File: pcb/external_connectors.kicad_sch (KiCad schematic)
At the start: 9 parts, among them J10 Conn_01x03_Pin, J11 Conn_01x03_Pin, J12 Conn_01x03_Pin, J13 Conn_01x03_Pin, J14 Conn_01x03_Pin, J15 Conn_02x10_Counter_Clockwise, J7 Conn_01x04_Pin_P2.54mm, J8 Conn_01x04_Qwiic, J9 Conn_01x03_Pin

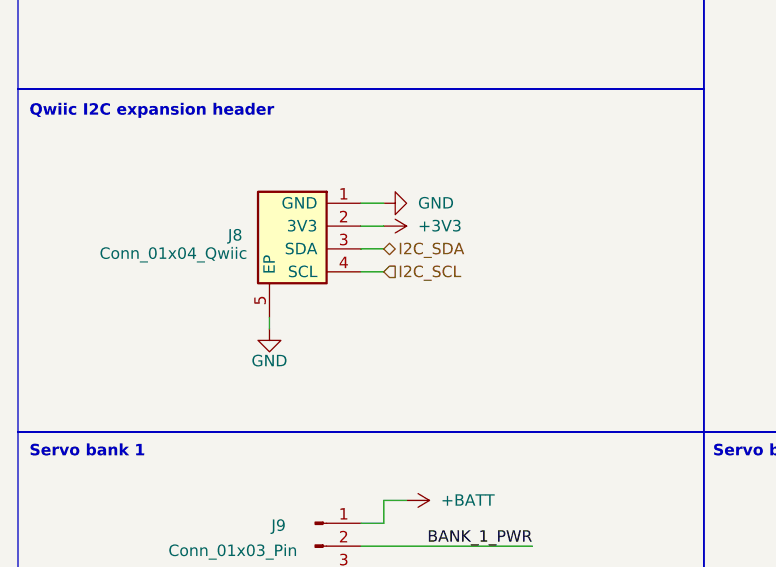
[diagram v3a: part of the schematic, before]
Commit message: Assign more footprints
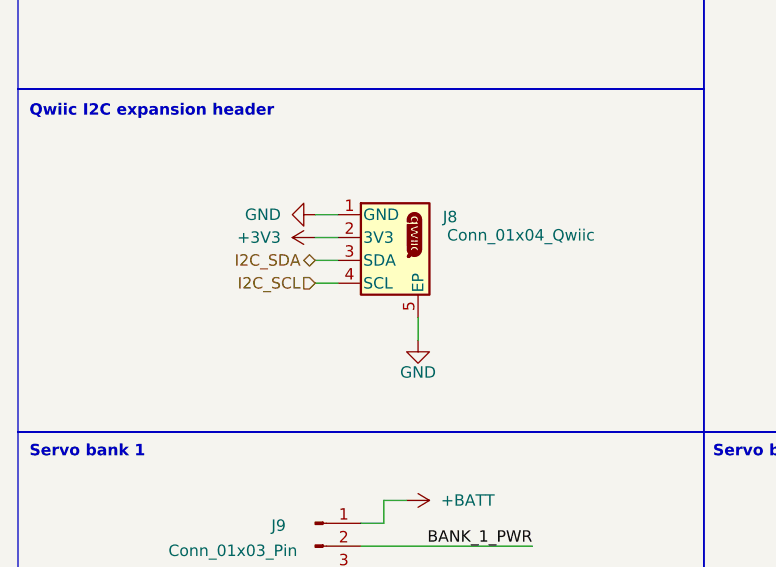
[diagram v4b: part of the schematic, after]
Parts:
- J8: footprint (none) -> Connector_JST:JST_SH_BM04B-SRSS-TB_1x04-1MP_P1.00mm_Vertical
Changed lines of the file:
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@@
 	(wire
 		(pts
-			(xy 50.8 71.12) (xy 53.34 71.12)
+			(xy 48.26 72.39) (xy 45.72 72.39)
 		)
 		(stroke
@@
 	(wire
 		(pts
-			(xy 40.64 77.47) (xy 40.64 76.2)
+			(xy 57.15 78.74) (xy 57.15 76.2)
 		)
 		(stroke
@@
 	(wire
 		(pts
-			(xy 50.8 66.04) (xy 53.34 66.04)
+			(xy 48.26 67.31) (xy 45.72 67.31)
 		)
 		(stroke
@@
 	(wire
 		(pts
-			(xy 50.8 68.58) (xy 53.34 68.58)
+			(xy 48.26 69.85) (xy 45.72 69.85)
 		)
 		(stroke
@@
 	(wire
 		(pts
-			(xy 50.8 63.5) (xy 53.34 63.5)
+			(xy 48.26 64.77) (xy 45.72 64.77)
 		)
 		(stroke
@@
 	(hierarchical_label "I2C_SCL"
 		(shape input)
-		(at 53.34 71.12 0)
+		(at 45.72 72.39 180)
 		(effects
 			(font
 				(size 1.27 1.27)
 			)
-			(justify left)
+			(justify right)
 		)
 	)
 	(hierarchical_label "I2C_SDA"
 		(shape bidirectional)
-		(at 53.34 68.58 0)
+		(at 45.72 69.85 180)
 		(effects
 			(font
 				(size 1.27 1.27)
 			)
-			(justify left)
+			(justify right)
 		)
 	)
@@
 	(symbol
 		(lib_id "Qwiic:Conn_01x04_Qwiic")
-		(at 45.72 66.04 0)
-		(mirror y)
+		(at 50.8 63.5 0)
 		(unit 1)
 		(exclude_from_sim no)
@@
 		(dnp no)
 		(property "Reference" "J8"
-			(at 36.83 67.056 0)
+			(at 60.706 65.024 0)
 			(effects
 				(font
@@
 		)
 		(property "Value" "Conn_01x04_Qwiic"
-			(at 29.972 69.088 0)
-			(effects
-				(font
-					(size 1.27 1.27)
-				)
-			)
-		)
-		(property "Footprint" ""
-			(at 45.72 66.04 0)
+			(at 68.58 67.056 0)
+			(effects
+				(font
+					(size 1.27 1.27)
+				)
+			)
+		)
+		(property "Footprint" "Connector_JST:JST_SH_BM04B-SRSS-TB_1x04-1MP_P1.00mm_Vertical"
+			(at 50.8 63.5 0)
 			(effects
 				(font
@@
 		)
 		(property "Datasheet" ""
-			(at 45.72 66.04 0)
-			(effects
-				(font
-					(size 1.27 1.27)
-				)
-				(hide yes)
-			)
-		)
-		(property "Description" "Qwiic I2C connector 4 pin"
-			(at 46.228 60.452 0)
+			(at 50.8 63.5 0)
+			(effects
+				(font
+					(size 1.27 1.27)
+				)
+				(hide yes)
+			)
+		)
+		(property "Description" "Qwiic I2C connector 4 pin, JST SH BM04B or JST SH SM04B"
+			(at 50.292 57.912 0)
 			(effects
 				(font
@@
 	(symbol
 		(lib_id "power:GND")
-		(at 53.34 63.5 90)
+		(at 45.72 64.77 270)
+		(mirror x)
 		(unit 1)
 		(exclude_from_sim no)
@@
 		(fields_autoplaced yes)
 		(property "Reference" "#PWR087"
-			(at 59.69 63.5 0)
+			(at 39.37 64.77 0)
 			(effects
 				(font
@@
 		)
 		(property "Value" "GND"
-			(at 57.15 63.4999 90)
+			(at 41.91 64.7699 90)
 			(effects
 				(font
@@
 		)
 		(property "Footprint" ""
-			(at 53.34 63.5 0)
+			(at 45.72 64.77 0)
 			(effects
 				(font
@@
 		)
 		(property "Datasheet" ""
-			(at 53.34 63.5 0)
+			(at 45.72 64.77 0)
 			(effects
 				(font
@@
 		)
 		(property "Description" "Power symbol creates a global label with name \"GND\" , ground"
-			(at 53.34 63.5 0)
+			(at 45.72 64.77 0)
 			(effects
 				(font
@@
 	(symbol
 		(lib_id "power:GND")
-		(at 40.64 77.47 0)
+		(at 57.15 78.74 0)
+		(mirror y)
 		(unit 1)
 		(exclude_from_sim no)
@@
 		(dnp no)
 		(property "Reference" "#PWR084"
-			(at 40.64 83.82 0)
+			(at 57.15 85.09 0)
 			(effects
 				(font
@@
 		)
 		(property "Value" "GND"
-			(at 40.64 81.026 0)
+			(at 57.15 82.296 0)
 			(effects
 				(font
@@
 		)
 		(property "Footprint" ""
-			(at 40.64 77.47 0)
+			(at 57.15 78.74 0)
 			(effects
 				(font
@@
 		)
 		(property "Datasheet" ""
-			(at 40.64 77.47 0)
+			(at 57.15 78.74 0)
 			(effects
 				(font
@@
 		)
 		(property "Description" "Power symbol creates a global label with name \"GND\" , ground"
-			(at 40.64 77.47 0)
+			(at 57.15 78.74 0)
 			(effects
 				(font
@@
 	(symbol
 		(lib_id "power:+3V3")
-		(at 53.34 66.04 270)
+		(at 45.72 67.31 90)
+		(mirror x)
 		(unit 1)
 		(exclude_from_sim no)
@@
 		(fields_autoplaced yes)
 		(property "Reference" "#PWR088"
-			(at 49.53 66.04 0)
+			(at 49.53 67.31 0)
 			(effects
 				(font
@@
 		)
 		(property "Value" "+3V3"
-			(at 57.15 66.0399 90)
+			(at 41.91 67.3099 90)
 			(effects
 				(font
@@
 		)
 		(property "Footprint" ""
-			(at 53.34 66.04 0)
+			(at 45.72 67.31 0)
 			(effects
 				(font
@@
 		)
 		(property "Datasheet" ""
-			(at 53.34 66.04 0)
+			(at 45.72 67.31 0)
 			(effects
 				(font
@@
 		)
 		(property "Description" "Power symbol creates a global label with name \"+3V3\""
-			(at 53.34 66.04 0)
-			(effects
-				(font
+			(at 45.72 67.31 0)
+			(effects
+				(font
